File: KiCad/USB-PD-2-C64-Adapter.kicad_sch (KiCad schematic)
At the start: 0 parts

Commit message: 5V-Zweig fertig: AP64500-Buck, Schutz, 3D-Modelle, BOM/Lib konsolidiert
- 5V-Strang komplett auf AP64500SP-13 (C2070920) umgestellt, RT6318C entfernt (Symbole/Datasheet/Altdateien geloescht)

- U1-Footprint korrigiert auf SOIC-8-1EP EP2.62x3.51mm_ThermalVias; Projekt-Library .pretty + .3dshapes angelegt

- 3D-Modelle fuer U1 (SOIC-8-1EP STEP) und F1 (Littelfuse OMNI-BLOK STEP) eingebunden, PCB direkt gepatcht

- BOM CSV/TXT, copilot-instructions und KiCad-Symbole konsistent mit Schaltplan; fp-lib-table + Datasheets ergaenzt
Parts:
- added C1: 47uF, Capacitor_SMD:CP_Elec_6.3x5.8, symbol Device:C_Polarized
- added C10: 220uF, Capacitor_SMD:CP_Elec_6.3x7.7, symbol Device:C_Polarized
- added C11: 100nF, Capacitor_SMD:C_0603_1608Metric, symbol Device:C
- added C12: 1nF, Capacitor_SMD:C_0603_1608Metric, symbol Device:C
- added C13, C6, C7, C8, C9: 22uF, Capacitor_SMD:C_1210_3225Metric, symbol Device:C
- added C2, C3: 10uF, Capacitor_SMD:C_1210_3225Metric, symbol Device:C
- added C4: 100nF BST-SW, Capacitor_SMD:C_0603_1608Metric, symbol Device:C
- added C5: 1.5nF, Capacitor_SMD:C_0603_1608Metric, symbol Device:C
- added D1: SMBJ18A TVS 18V VRWM, Diode_SMD:D_SMB, symbol Device:D_TVS
- added F1: JFC2410-1400TS 4A 250V 2410 fuse, USB-PD-2-C64-Adapter:XFCN_XF-155_2410_FuseHolder, symbol Device:Fuse
- added J1: PD controller 15V/3A in, TBD, symbol Connector_Generic:Conn_01x02
- added J2: C64 DIN 5V pins, Connector_DIN:DIN-7, symbol USB-PD-2-C64-Adapter:C64_DIN_5V_OUT
- added L1: 2.2uH MWSA0603S, Inductor_SMD:L_Sunlord_MWSA0603S, symbol Device:L
- added R1: 66.5k RT 1.5MHz, Resistor_SMD:R_0603_1608Metric, symbol Device:R
- added R2: 39.2k, Resistor_SMD:R_0603_1608Metric, symbol Device:R
- added R3: 105k 0.1%, Resistor_SMD:R_0603_1608Metric, symbol Device:R
- added R4: 20.0k 0.1%, Resistor_SMD:R_0603_1608Metric, symbol Device:R
- added R5: 124k 0.1%, Resistor_SMD:R_0603_1608Metric, symbol Device:R
- added R6: 10k 0.1%, Resistor_SMD:R_0603_1608Metric, symbol Device:R
- added R7: 33, Resistor_SMD:R_0603_1608Metric, symbol Device:R
- added U1: AP64500SP-13, USB-PD-2-C64-Adapter:SOIC-8-1EP_3.9x4.9mm_P1.27mm_EP2.62x3.51mm_ThermalVias, symbol USB-PD-2-C64-Adapter:AP64500SP-13
- added U2: STEF05SGR, Package_TO_SOT_SMD:TSOT-23-8, symbol USB-PD-2-C64-Adapter:STEF05S
- added U3: TPS3700DDCR, Package_TO_SOT_SMD:SOT-23-6, symbol dk_Linear-Comparators:TPS3700DDCR
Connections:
- new net: C12.1, R5.2, R6.1, U3.4 (INB-)
- new net: C4.1, U1.1 (BST)
- new net: R1.1, U1.4 (RT/CLK)
- new net: R7.1, U2.1 (ILim)
- new net: U2.2 (En/Fault), U3.6 (OUTB)
- new net 5V_PROTECTED_SENSE: C13.1, J2.1 (+5V), R7.2, U2.5 (VOUT), U2.6 (VOUT)
- new net 5V_RAW: C10.1, C11.1, C5.1, C6.1, C7.1, C8.1, C9.1, L1.2, R3.1, R5.1, U2.7 (VCC), U2.8 (VCC), U3.3 (INA+), U3.5 (VDD)
- new net BUCK_EN: C1.1, C2.1, C3.1, D1.2 (A2), F1.2, U1.2 (VIN), U1.3 (EN/UVLO)
- new net COMP: R2.1, U1.6 (COMP)
- new net FB: C5.2, R3.2, R4.1, U1.5 (FB)
- new net GND: C1.2, C10.2, C11.2, C12.2, C13.2, C2.2, C3.2, C6.2, C7.2, C8.2, C9.2, D1.1 (A1), J1.1 (Pin_1), J2.2 (GND), R1.2, R2.2, R4.2, R6.2, U1.7 (GND), U2.4 (GND), U3.2 (GND)
- new net SW: C4.2, L1.1, U1.8 (SW)
- new net VIN_PD_15V: F1.1, J1.2 (Pin_2)
- no-connect marks 0 -> 1
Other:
- note added: "2x 10uF X7R 50V"
- note added: "4x 22uF X7R 25V"
- note added: "AP64500 first-pass values: fSW 1.5MHz, L1 2.2uH Isat >=7A, COUT local 4x22uF X7R + 150..220uF polymer."
- note added: "Input protection: 15V-PD fixed input; D1 planned as SMBJ18A, verify clamp/energy with fuse or input eFuse."
- title: (none) -> USB-PD-2-C64-Adapter - 5V DC Branch

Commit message: Update USB-PD input protection assets
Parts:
- removed C3: 10uF, Capacitor_SMD:C_1210_3225Metric, symbol Device:C
- removed R7: 33, Resistor_SMD:R_0603_1608Metric, symbol Device:R
- removed U2: STEF05SGR, Package_TO_SOT_SMD:TSOT-23-8, symbol USB-PD-2-C64-Adapter:STEF05S
- added C14: 1uF X7R 25V, Capacitor_SMD:C_0603_1608Metric, symbol Device:C
- added C15: 100nF X7R 50V, Capacitor_SMD:C_0603_1608Metric, symbol Device:C
- added C16: 22nF X7R 50V, Capacitor_SMD:C_0603_1608Metric, symbol Device:C
- added D2: KT-0603G green, USB-PD-2-C64-Adapter:KT-0603G_C12624, symbol USB-PD-2-C64-Adapter:KT-0603G
- added J3: TYPE-C16PIN C393939, USB-PD-2-C64-Adapter:TYPE-C16PIN_C393939, symbol USB-PD-2-C64-Adapter:TYPE-C16PIN_C393939
- added R10: 2.2k, Resistor_SMD:R_0603_1608Metric, symbol Device:R
- added R11: 1M, Resistor_SMD:R_0603_1608Metric, symbol Device:R
- added R12, R13: 100k, Resistor_SMD:R_0603_1608Metric, symbol Device:R
- added R14: 274k, Resistor_SMD:R_0603_1608Metric, symbol Device:R
- added R15: 7.68k, Resistor_SMD:R_0603_1608Metric, symbol Device:R
- added R16: 20.0k, Resistor_SMD:R_0603_1608Metric, symbol Device:R
- added R17: 18k, Resistor_SMD:R_0603_1608Metric, symbol Device:R
- added R8: 56k 1%, Resistor_SMD:R_0603_1608Metric, symbol Device:R
- added R9: 1k 1%, Resistor_SMD:R_1206_3216Metric, symbol Device:R
- added U4: CH224K, USB-PD-2-C64-Adapter:CH224K_ESSOP-10-150mil-1mm, symbol USB-PD-2-C64-Adapter:CH224K
- added U5: TPD2S300YFFR, USB-PD-2-C64-Adapter:TPD2S300YFFR_DSBGA-9, symbol USB-PD-2-C64-Adapter:TPD2S300YFFR
- added U6: TPS16630PWPR, Package_SO:HTSSOP-20-1EP_4.4x6.5mm_P0.65mm_EP3.0x4.2mm, symbol USB-PD-2-C64-Adapter:TPS16630PWPR
- J1: value PD controller 15V/3A in -> 2-pin 2.54mm lab/test input DNP; footprint TBD -> Connector_PinHeader_2.54mm:PinHeader_1x02_P2.54mm_Vertical; LCSC TBD -> DNP
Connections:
- net 5V_RAW is gone; now on net 5V_PROTECTED_SENSE: C10.1, C11.1, C5.1, C6.1, C7.1, C8.1, C9.1, L1.2, R3.1, R5.1, U3.3 (INA+), U3.5 (VDD)
- net BUCK_EN: now also R11.2, R12.1; no longer C1.1, C2.1, D1.2 (A2), F1.2, U1.2 (VIN)
- net GND: now also C14.2, C15.2, C16.2, D2.2 (A), J3.A1B12 (GND_A1B12), J3.B1A12 (GND_B1A12), J3.SH (SHELL), R12.2, R16.2, R17.2, R8.1, U4.11 (GND_EP), U5.B2 (GND), U6.21 (PowerPAD/GND), U6.9 (GND)
- net EFUSE_SHDN: now reaches U3.6 (OUTB)
- net EFUSE_SHDN: now also R13.1, U6.13 (SHDN)
- net VIN_PD_15V: no longer names the net of F1.1
- net VIN_PD_15V: now also J3.A4B9 (VBUS_A4B9), J3.B4A9 (VBUS_B4A9); no longer J1.2 (Pin_2)
- new net: C16.1, U6.10 (dVdT)
- new net: R17.1, U6.11 (ILIM)
- new net: R14.2, R15.1, U6.7 (UVLO)
- new net: R15.2, R16.1, U6.8 (OVP)
- new net: J3.A5 (CC1_A5), U5.A1 (C_CC1)
- new net: J3.B5 (CC2_B5), U5.A3 (C_CC2)
- new net: R10.1, U4.10 (PG)
- new net: U4.6 (CC2), U5.B3 (CC2)
- new net: U4.7 (CC1), U5.B1 (CC1)
- new net: R8.2, U4.9 (CFG1)
- new net: D2.1 (K), R10.2
- new net CH224_VDD_3V3: C14.1, R13.2, R9.2, U4.1 (VDD), U5.C2 (VPWR), U5.C3 (VM)
- new net TPD_VBIAS: C15.1, U5.A2 (VBIAS)
- new net VBUS: F1.2, J1.2 (Pin_2), R14.1, R9.1, U4.8 (VBUS), U6.1 (IN), U6.2 (IN), U6.3 (IN), U6.6 (P_IN)
- new net VIN_BUCK: C1.1, C2.1, D1.2 (A2), R11.1, U1.2 (VIN), U6.18 (OUT), U6.19 (OUT), U6.20 (OUT)
- no-connect marks 1 -> 16
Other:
- note removed: "2x 10uF X7R 50V"
- note removed: "AP64500 first-pass values: fSW 1.5MHz, L1 2.2uH Isat >=7A, COUT local 4x22uF X7R + 150..220uF polymer."
- note removed: "Input protection: 15V-PD fixed input; D1 planned as SMBJ18A, verify clamp/energy with fuse or input eFuse."
- moved on the sheet: C1, C10, C11, C12, C13, C2, C4, C5, C6, C7, C8, C9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

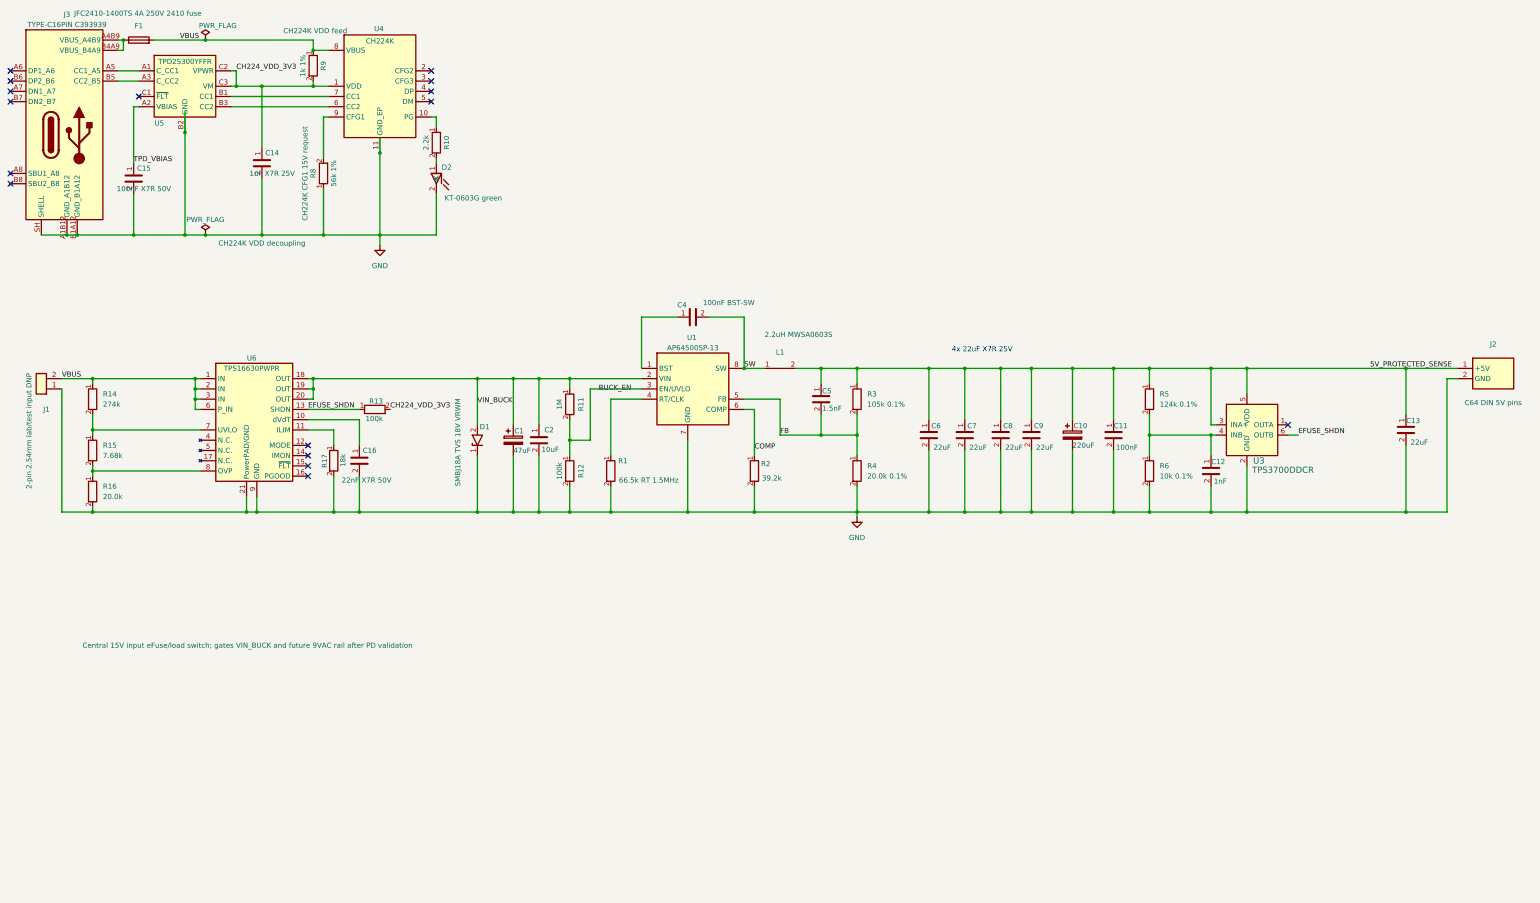
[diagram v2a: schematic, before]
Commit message: Update 9VAC design assets
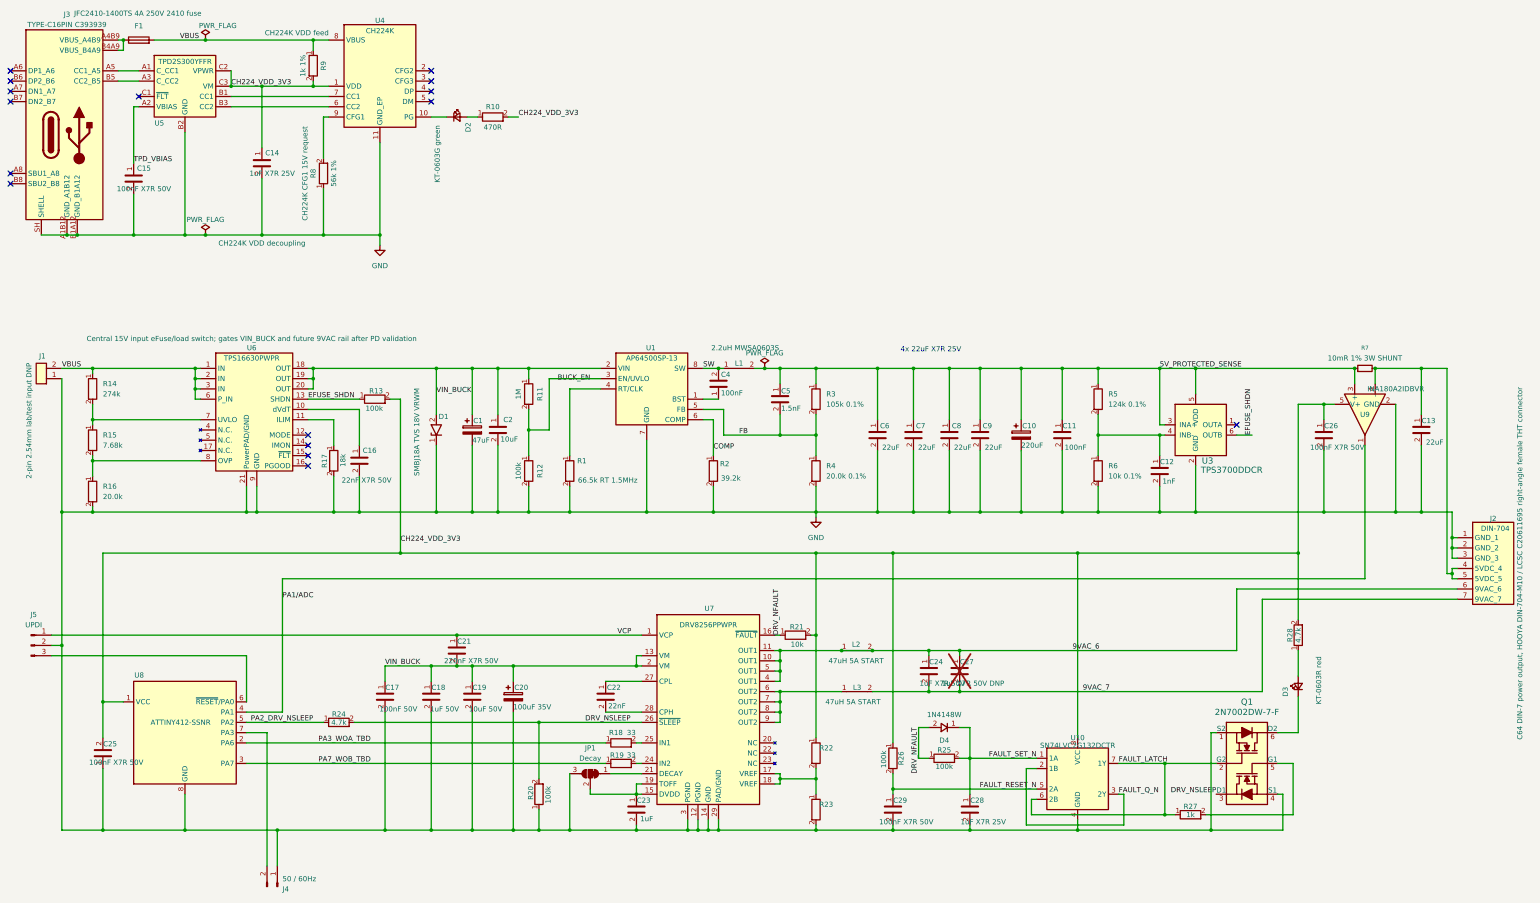
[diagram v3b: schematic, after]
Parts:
- added C17: 100nF 50V, Capacitor_SMD:C_0603_1608Metric, symbol Device:C
- added C18: 1uF 50V, Capacitor_SMD:C_0805_2012Metric, symbol Device:C
- added C19: 10uF 50V, Capacitor_SMD:C_1210_3225Metric, symbol Device:C
- added C20: 100uF 35V, Capacitor_SMD:CP_Elec_6.3x7.7, symbol Device:C_Polarized
- added C21: 220nF X7R 50V, Capacitor_SMD:C_0603_1608Metric, symbol Device:C
- added C22: 22nF, Capacitor_SMD:C_0603_1608Metric, symbol Device:C
- added C23: 1uF, Capacitor_SMD:C_0603_1608Metric, symbol Device:C
- added C24: 1uF X7R 50V, Capacitor_SMD:C_1210_3225Metric, symbol Device:C
- added C25, C26, C29: 100nF X7R 50V, Capacitor_SMD:C_0603_1608Metric, symbol Device:C
- added C27: 1uF X7R 50V DNP, Capacitor_SMD:C_1210_3225Metric, symbol Device:C
- added C28: 1uF X7R 25V, Capacitor_SMD:C_0603_1608Metric, symbol Device:C
- added D3: KT-0603R red, LED_SMD:LED_0603_1608Metric, symbol USB-PD-2-C64-Adapter:LED_Small
- added D4: 1N4148W, Diode_SMD:D_SOD-123, symbol USB-PD-2-C64-Adapter:1N4148W
- added J4: 50 / 60Hz, Connector_PinHeader_2.54mm:PinHeader_1x02_P2.54mm_Vertical, symbol Connector:Conn_01x02_Pin
- added J5: UPDI, Connector_PinHeader_2.54mm:PinHeader_1x03_P2.54mm_Vertical, symbol Connector:Conn_01x03_Pin
- added JP1: Decay, Jumper:SolderJumper-3_P1.3mm_Bridged12_RoundedPad1.0x1.5mm, symbol Jumper:SolderJumper_3_Bridged12
- added L2, L3: 47uH 5A START, Inductor_SMD:L_10.4x10.4_H4.8, symbol Device:L
- added Q1: 2N7002DW-7-F, digikey-footprints:SOT-363, symbol dk_Transistors-FETs-MOSFETs-Arrays:2N7002DW-7-F
- added R18, R19: 33, Resistor_SMD:R_0603_1608Metric, symbol Device:R
- added R20, R25, R26: 100k, Resistor_SMD:R_0603_1608Metric, symbol Device:R
- added R21: 10k, Resistor_SMD:R_0603_1608Metric, symbol Device:R
- added R22, R23: 10k 1%, Resistor_SMD:R_0603_1608Metric, symbol Device:R
- added R24, R28: 4.7k, Resistor_SMD:R_0603_1608Metric, symbol Device:R
- added R27: 1k, Resistor_SMD:R_0603_1608Metric, symbol Device:R
- added R7: 10mR 1% 3W SHUNT, Resistor_SMD:R_2512_6332Metric, symbol Device:R_Small
- added U10: SN74LVC2G132DCTR, Package_SO:VSSOP-8_3x3mm_P0.65mm, symbol USB-PD-2-C64-Adapter:SN74LVC2G132DCTR
- added U7: DRV8256PPWPR, Package_SO:Texas_PWP0028V_TSSOP-28-1EP_4.4x9.7mm_P0.65mm_EP3.4x9.7mm_Mask2.94x5.62mm_ThermalVias, symbol USB-PD-2-C64-Adapter:DRV8256PPWPR
- added U8: ATTINY412-SSNR, Package_SO:SOIC-8_3.9x4.9mm_P1.27mm, symbol MCU_Microchip_ATtiny:ATtiny412-SS
- added U9: INA180A2IDBVR, Package_TO_SOT_SMD:SOT-23-5, symbol Amplifier_Current:INA180A2
- C16: LCSC TBD -> C106222
- C4: value 100nF BST-SW -> 100nF
- D2: symbol USB-PD-2-C64-Adapter:KT-0603G -> USB-PD-2-C64-Adapter:LED_Small
- J2: value C64 DIN 5V pins -> DIN-704; footprint Connector_DIN:DIN-7 -> USB-PD-2-C64-Adapter:DIN-704-M10_C20611695; LCSC TBD -> C20611695
- R10: value 2.2k -> 470R; LCSC C114662 -> C23179
- R14: LCSC TBD -> C482818
- R15: LCSC TBD -> C163419
- R17: LCSC TBD -> C114610
- U6: LCSC TBD -> C1849461
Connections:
- net 5V_PROTECTED_SENSE: now also R7.1, U9.3 (+); no longer C13.1, J2.1 (+5V)
- net CH224_VDD_3V3: now also R10.2, C25.2, C26.1, R21.2, R22.1, R26.1, R28.2, U10.8 (VCC), U8.1 (VCC), U9.5 (V+)
- net GND: now also J2.1 (GND_1), J2.3 (GND_3), C17.2, C18.2, C19.2, C20.2, C23.2, C25.1, C26.2, C28.2, C29.2, J4.1 (Pin_1), J5.2 (Pin_2), JP1.3 (B), Q1.1 (S2), Q1.4 (S1), R20.1, R23.2, U10.4 (GND), U7.12 (PGND), U7.14 (GND), U7.29 (PAD/GND), U7.3 (PGND), U8.8 (GND), U9.2 (GND); no longer D2.2 (A)
- net VIN_BUCK: now also C17.1, C18.1, C19.1, C20.1, C21.2, U7.13 (VM), U7.2 (VM)
- net at U4.10 (PG): now also D2.1 (K); no longer R10.1
- new net: C13.1, J2.4 (5VDC_4), J2.5 (5VDC_5), R7.2, U9.4 (-)
- new net: D2.2 (A), R10.1
- new net: JP1.1 (A), U7.21 (DECAY)
- new net: C23.1, JP1.2 (C), U7.15 (DVDD), U7.19 (TOFF)
- new net: R22.2, R23.1, U7.17 (VREF), U7.18 (VREF)
- new net: R19.2, U7.24 (IN2)
- new net: R18.2, U7.25 (IN1)
- new net: C22.1, U7.27 (CPL)
- new net: C22.2, U7.28 (CPH)
- new net: L3.1, U7.6 (OUT2), U7.7 (OUT2), U7.8 (OUT2), U7.9 (OUT2)
- new net: D3.1 (K), Q1.6 (D2)
- new net: D3.2 (A), R28.1
- new net: Q1.5 (G1), R27.2
- new net: J4.2 (Pin_2), U8.7 (PA3)
- new net: J5.3 (Pin_3), U8.6 (~{RESET}/PA0)
- new net 9VAC_6: C24.1, C27.1, J2.6 (9VAC_6), L2.1, L2.2, U7.10 (OUT1), U7.11 (OUT1), U7.4 (OUT1), U7.5 (OUT1)
- new net 9VAC_7: C24.2, C27.2, J2.7 (9VAC_7), L3.2
- new net DRV_NFAULT: D4.2 (A), R21.1, R25.1, U7.16 (~{FAULT})
- new net DRV_NSLEEP: Q1.3 (D1), R20.2, R24.2, U7.26 (~{SLEEP})
- new net FAULT_LATCH: Q1.2 (G2), R27.1, U10.6 (2B), U10.7 (1Y)
- new net FAULT_Q_N: U10.2 (1B), U10.3 (2Y)
- new net FAULT_RESET_N: C29.1, R26.2, U10.5 (2A)
- new net FAULT_SET_N: C28.1, D4.1 (K), R25.2, U10.1 (1A)
- new net PA1/ADC: U8.4 (PA1), U9.1
- new net PA2_DRV_NSLEEP: R24.1, U8.5 (PA2)
- new net PA3_WOA_TBD: R18.1, U8.2 (PA6)
- new net PA7_WOB_TBD: R19.1, U8.3 (PA7)
- new net VCP: C21.1, J5.1 (Pin_1), U7.1 (VCP)
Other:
- moved on the sheet: C1, C10, C11, C12, C13, C2, C4, C5, C6, C7, C8, C9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
